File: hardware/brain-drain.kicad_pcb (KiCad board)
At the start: 4 copper layers, 150 x 122 mm, 167 parts, among them J10 bay slot 1, J11 bay slot 2, J12 bay slot 3, J13 bay slot 4, J14 bay slot 5, J15 bay slot 6, J16 bay slot 7, J17 bay slot 8, J21 KPJX-4S-S, J3 microSD, J40 Fan GND/5V/TACH/PWM, J41 OLED GND/VCC/SCL/SDA, J5 USB-C rpiboot, J50 M.2 M-key, J6 nRPIBOOT, J7 UART0 GND/TX/RX, M1 CM5002016, Q20 AO4407A, SW1 DIP x8, SW3 lid microswitch, U1 USB5744/2G, U2 USB5744/2G, U20 TPS56637RPAR, U21 TPS56637RPAR, U22 AP63203WU-7, U3 AP2112K-1.2, U50 TPS22965DSGR, U51 AP63203WU-7, U52 TPS22965DSGR, Y1 25MHz CL=20pF, Y2 25MHz CL=20pF

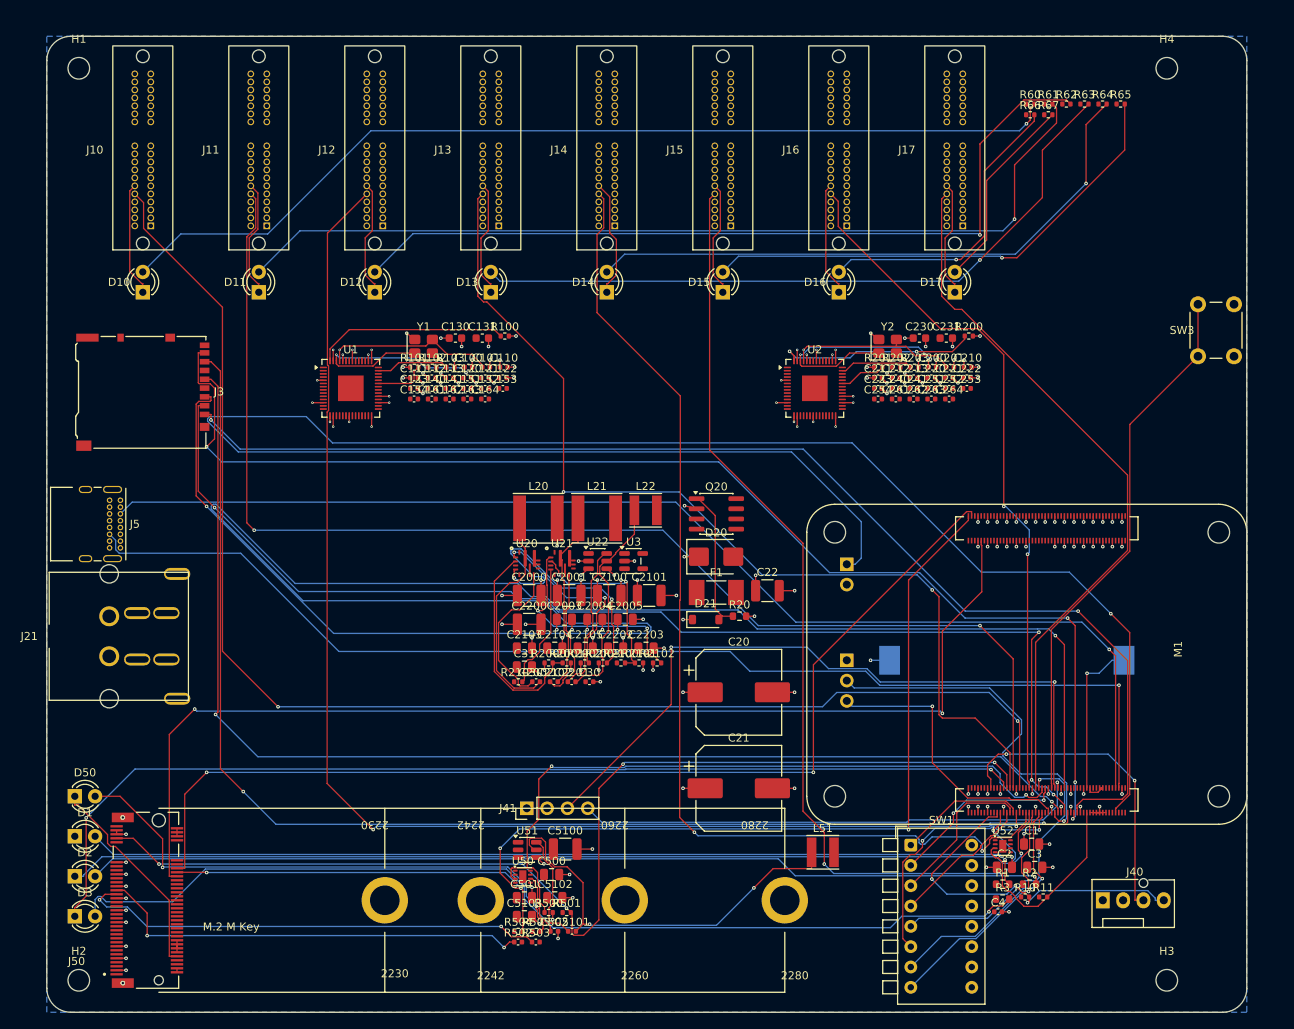
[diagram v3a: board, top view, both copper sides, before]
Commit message: hw(brain): first full chain — 49 open (31 plane pins, 18 pair ends) before the Q20 pin fix; Q20 re-netted, chain relaunched
Co-Authored-By: Claude Sonnet 5 <noreply@anthropic.com>
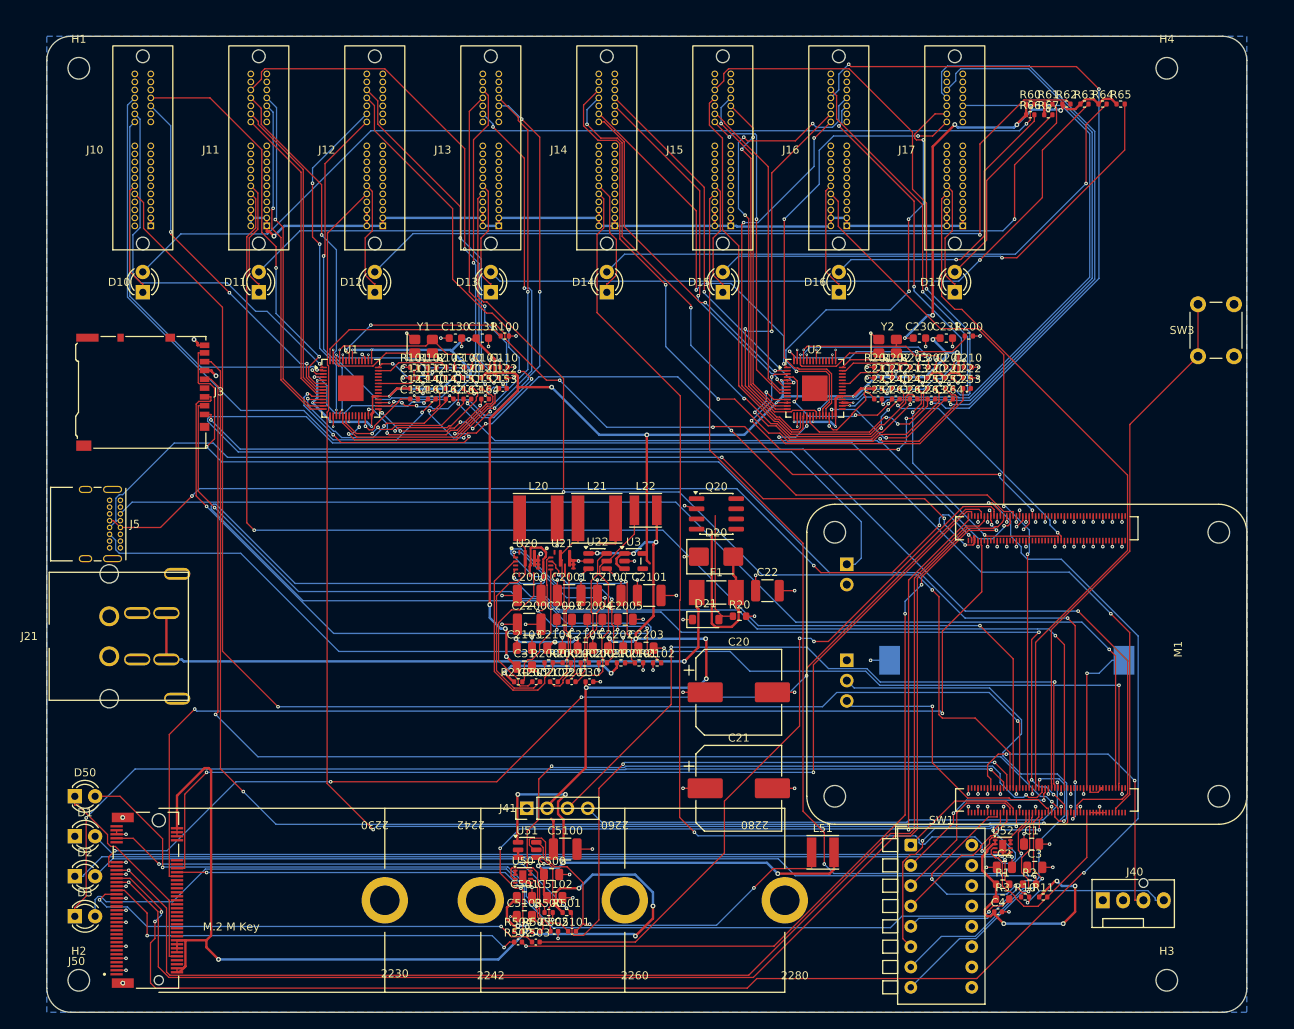
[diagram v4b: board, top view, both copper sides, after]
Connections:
- Q20 pad 1: Q20_GATE -> +12V
- Q20 pad 3: VIN_12V_FUSED -> +12V
- Q20 pad 4: (no net) -> Q20_GATE
- Q20 pad 5: (no net) -> VIN_12V_FUSED
- Q20 pad 6: (no net) -> VIN_12V_FUSED
- Q20 pad 7: (no net) -> VIN_12V_FUSED
- Q20 pad 8: (no net) -> VIN_12V_FUSED
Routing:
- net +1V2: track 18.2 -> 223.7 mm, vias 16 -> 25
- net PCIE_TX_P: track 0.00 -> 201.9 mm, vias 0 -> 4
- net +3V3: track 20.7 -> 199.3 mm, vias 20 -> 37
- net PCIE_TX_N: track 0.00 -> 162.5 mm, vias 0 -> 1
- net PCIE_CLK_N: track 0.00 -> 161.1 mm, vias 0 -> 1
- net PCIE_CLK_P: track 0.00 -> 130.4 mm, vias 0 -> 4
- net 3V3_M2_SW: track 3.50 -> 132.3 mm, vias 0 -> 6
- net +12V: track 24.1 -> 146.7 mm, vias 14 -> 16
- net USB2_DP: track 0.00 -> 122.1 mm, vias 0 -> 3
- net USB2_DM: track 0.00 -> 119.5 mm, vias 0 -> 4
- net PCIE_RX_P: track 0.00 -> 100.1 mm, vias 0 -> 6
- net USB3_0_TX_P: track 0.00 -> 99.6 mm, vias 0 -> 6
- net PCIE_RX_N: track 0.00 -> 90.8 mm, vias 0 -> 2
- net BAY7_USB3_RX_N: track 0.00 -> 90.0 mm, vias 0 -> 3
- net USB3_0_RX_P: track 0.00 -> 89.2 mm, vias 0 -> 4
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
